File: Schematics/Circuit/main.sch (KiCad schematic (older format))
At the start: 49 parts

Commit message: Edit schematic and model
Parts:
- removed C?: 2.2 nF, ~, symbol C
- removed C?: 0.8 uF, ~, symbol C
- removed C?: 100 nF, ~, symbol C
- removed C?: 10 nF, ~, symbol C
- removed IC?: MPU-6050, ~, symbol MPU-6050
- removed R?: 4k7, ~, symbol R
- added J1, J2, J3, J4, J5: Conn_01x07, symbol Conn_01x07
- added R10, R11, R12, R13, R5, R6, R7, R8: 10k, symbol R
- added R14, R16, R18: 2k2, symbol R
- added R15, R17, R19: 2k8, symbol R
- C1, C10, C11, C12, C13, C2, C3, C4, C5, C8, C9: renamed from C?; symbol C -> C-RESCUE-main
- C6, C7: renamed from C?; value 22 pF -> 20 pF; symbol C -> C-RESCUE-main
- R1, R4: renamed from R?; symbol R -> R-RESCUE-main
- R2, R3: renamed from R?; value 4k7 -> 2k; symbol R -> R-RESCUE-main
- gave numbers to parts that had none: 26
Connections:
- net labels added: INT1, INT2, INT3, INT4, LED-TOP, LED1, LED2, LED3, LED4, PWRKEY, RXD-GSM, SLEEP-GSM, TXD-GSM, XSHUT1, XSHUT2, XSHUT3, XSHUT4
- wire segments 144 -> 170
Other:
- moved on the sheet: C10, C11, C12, C13, C6, C7, CSTECE1, IC3, P18, P19, R4

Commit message: Edit schematic and footprints
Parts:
- added J1: Conn_01x03, Pin_Headers:Pin_Header_Straight_1x03_Pitch2.54mm, symbol Conn_01x03
- C1, C3, C5, C8: footprint ~ -> Capacitors_Tantalum_SMD:CP_Tantalum_Case-C_EIA-6032-28_Hand
- C10, C11, C12, C13, C2, C4, C9: footprint ~ -> Capacitors_SMD:C_0805_HandSoldering
- C6, C7: footprint ~ -> Capacitors_SMD:C_0402
- CSTECE1: footprint ~ -> Crystals:Crystal_SMD_SeikoEpson_MA505-2pin_12.7x5.1mm_HandSoldering
- D1: footprint ~ -> Diodes_SMD:D_MiniMELF_Handsoldering
- IC1, IC2: footprint (none) -> CanSat:ncp1117
- IC3: footprint TQFP100 -> ATMEGA2560-16AU:QFP50P1600X1600X120-100N
- J2: renamed from J1; footprint (none) -> Pin_Headers:Pin_Header_Straight_1x07_Pitch2.54mm
- J3: renamed from J2; footprint (none) -> Pin_Headers:Pin_Header_Straight_1x07_Pitch2.54mm
- J4: renamed from J3; footprint (none) -> Pin_Headers:Pin_Header_Straight_1x07_Pitch2.54mm
- J5: renamed from J4; footprint (none) -> Pin_Headers:Pin_Header_Straight_1x07_Pitch2.54mm
- J6: renamed from J5; footprint (none) -> Pin_Headers:Pin_Header_Straight_1x07_Pitch2.54mm
- K1, K2: footprint (none) -> CanSat:SMD_6pin_IC
- P1, P10, P11, P12, P13, P14, P15, P16, P2, P3, P4, P5, P6, P7, P8, P9: footprint (none) -> Pin_Headers:Pin_Header_Straight_1x02_Pitch2.54mm
- P17: footprint (none) -> Pin_Headers:Pin_Header_Straight_2x05_Pitch2.00mm
- P18: footprint (none) -> CanSat:co2
- P19: footprint (none) -> Pin_Headers:Pin_Header_Straight_1x04_Pitch2.54mm
- R1, R2, R3, R4: footprint ~ -> Resistors_SMD:R_0603
- R10: renamed from R11; footprint (none) -> Resistors_SMD:R_0603
- R11: renamed from R12; footprint (none) -> Resistors_SMD:R_0603
- R12: renamed from R13; footprint (none) -> Resistors_SMD:R_0603
- R13: renamed from R14; footprint (none) -> Resistors_SMD:R_0805
- R14: renamed from R15; footprint (none) -> Resistors_SMD:R_0603
- R15: renamed from R16; footprint (none) -> Resistors_SMD:R_0805
- R16: renamed from R17; footprint (none) -> Resistors_SMD:R_0603
- R17: renamed from R18; footprint (none) -> Resistors_SMD:R_0805
- R18: renamed from R19; footprint (none) -> Resistors_SMD:R_0603
- R5, R6, R7, R8: footprint (none) -> Resistors_SMD:R_0603
- R9: renamed from R10; footprint (none) -> Resistors_SMD:R_0603
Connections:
- net labels added: SERVO
- wire segments 170 -> 178

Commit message: Edit finish circuits and some model work
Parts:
- removed P17: CONN_9, Pin_Headers:Pin_Header_Straight_2x05_Pitch2.00mm, symbol CONN_9
- added C14: 100 nF, Capacitors_SMD:C_0805, symbol C-RESCUE-main
- added IC4: RFM69HW, RFM69HW:XCVR_RFM95W-868S2, symbol RFM69HW
- added J10: Conn_01x04, CanSat:MOLEX_PicoBlade_4, symbol Conn_01x04
- added J7: Conn_01x05, Pin_Headers:Pin_Header_Straight_1x05_Pitch1.27mm_SMD_Pin1Right, symbol Conn_01x05
- added J8: Conn_02x05_Counter_Clockwise, Pin_Headers:Pin_Header_Straight_2x05_Pitch1.00mm_SMD, symbol Conn_02x05_Counter_Clockwise
- added J9: Conn_01x06, CanSat:MOLEX_PicoBlade_6, symbol Conn_01x06
- added P17, P20, P21: CONN_2, CanSat:MOLEX_PicoBlade_2, symbol CONN_2
- added Q1, Q2, Q3, Q4, Q5, Q6: BSS138, TO_SOT_Packages_SMD:SOT-23, symbol BSS138
- added R19, R20, R21, R22, R24, R25, R26, R28, R29, R30, R31, R32: 10k, Resistors_SMD:R_0603, symbol R
- added R23: 2k2, Resistors_SMD:R_0805, symbol R
- added R27: 2k8, Resistors_SMD:R_0603, symbol R
- added R33: 20k, Resistors_SMD:R_0603, symbol R-RESCUE-main
- added R34: 10k, Resistors_SMD:R_0603, symbol R-RESCUE-main
- C1: footprint Capacitors_Tantalum_SMD:CP_Tantalum_Case-C_EIA-6032-28_Hand -> Capacitors_Tantalum_SMD:CP_Tantalum_Case-U_EIA-6032-15_Reflow
- C10, C11, C12, C13, C2, C4, C9: footprint Capacitors_SMD:C_0805_HandSoldering -> Capacitors_SMD:C_0805
- C3, C5, C8: footprint Capacitors_Tantalum_SMD:CP_Tantalum_Case-C_EIA-6032-28_Hand -> Capacitors_Tantalum_SMD:CP_Tantalum_Case-C_EIA-6032-28_Reflow
- CSTECE1: footprint Crystals:Crystal_SMD_SeikoEpson_MA505-2pin_12.7x5.1mm_HandSoldering -> CanSat:Crystal_SMD
- D1: footprint Diodes_SMD:D_MiniMELF_Handsoldering -> Diodes_SMD:D_MiniMELF
- IC3: footprint ATMEGA2560-16AU:QFP50P1600X1600X120-100N -> CanSat:AtMega2560-AU
- J1: footprint Pin_Headers:Pin_Header_Straight_1x03_Pitch2.54mm -> MOLEX_PicoBlade_3:MOLEX_0532610371
- J2, J3, J4, J5, J6: footprint Pin_Headers:Pin_Header_Straight_1x07_Pitch2.54mm -> CanSat:MOLEX_PicoBlade_7
- P1, P10, P11, P12, P13, P14, P15, P16, P2, P3, P4, P5, P6, P7, P8, P9: footprint Pin_Headers:Pin_Header_Straight_1x02_Pitch2.54mm -> CanSat:MOLEX_PicoBlade_2
- P19: footprint Pin_Headers:Pin_Header_Straight_1x04_Pitch2.54mm -> CanSat:MOLEX_PicoBlade_4
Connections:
- net labels added: DTR, LED_TOP, MISO, MOSI, PWM1, PWM2, PWM3, PWM4, PWM5, PWM6, PWM7, PWM8, RFMINT, RFM_INT, SCK, SS, V_READ
- net labels removed: FC_IN, FC_OUT, LED, LED-TOP
- wire segments 178 -> 247
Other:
- moved on the sheet: J1, J2, K1, P18, P19, R13, R14, R15, R16, R17, R18

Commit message: Edit pcb and model
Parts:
- added J11: Conn_01x04, CanSat:MOLEX_PicoBlade_4, symbol Conn_01x04
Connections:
- net labels added: RX_GPS, TX_GPS
- wire segments 247 -> 253
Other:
- moved on the sheet: J1
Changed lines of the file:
@@
 	1    0    0    -1
 $EndComp
-Text Label 4200 5400 0    60   ~ 0
+Text Label 7100 5400 0    60   ~ 0
 TX
-Text Label 4200 5300 0    60   ~ 0
+Text Label 7100 5300 0    60   ~ 0
 RX
 Text Label 7050 4500 0    60   ~ 0
@@
 Text Label 10400 3000 0    60   ~ 0
 SLEEP-GSM
-Text Label 7050 5400 0    60   ~ 0
+Text Label 3950 5400 0    60   ~ 0
 RXD-GSM
-Text Label 7050 5300 0    60   ~ 0
+Text Label 3950 5300 0    60   ~ 0
 TXD-GSM
 Text Label 7050 4800 0    60   ~ 0
@@
 L Conn_01x03 J1
 U 1 1 5A54080E
-P 3900 4200
-F 0 "J1" H 3900 4400 50  0000 C CNN
-F 1 "Conn_01x03" H 3900 4000 50  0000 C CNN
-F 2 "MOLEX_PicoBlade_3:MOLEX_0532610371" H 3900 4200 50  0001 C CNN
-F 3 "" H 3900 4200 50  0001 C CNN
-	1    3900 4200
+P 3750 4200
+F 0 "J1" H 3750 4400 50  0000 C CNN
+F 1 "Conn_01x03" H 3750 4000 50  0000 C CNN
+F 2 "MOLEX_PicoBlade_3:MOLEX_0532610371" H 3750 4200 50  0001 C CNN
+F 3 "" H 3750 4200 50  0001 C CNN
+	1    3750 4200
 	1    0    0    -1
 $EndComp
@@
 L +5V #PWR049
 U 1 1 5A540AD7
-P 3450 4200
-F 0 "#PWR049" H 3450 4050 50  0001 C CNN
-F 1 "+5V" H 3450 4340 50  0000 C CNN
-F 2 "" H 3450 4200 50  0001 C CNN
-F 3 "" H 3450 4200 50  0001 C CNN
-	1    3450 4200
+P 3300 4200
+F 0 "#PWR049" H 3300 4050 50  0001 C CNN
+F 1 "+5V" H 3300 4340 50  0000 C CNN
+F 2 "" H 3300 4200 50  0001 C CNN
+F 3 "" H 3300 4200 50  0001 C CNN
+	1    3300 4200
 	0    -1   -1   0
 $EndComp
@@
 L GND #PWR050
 U 1 1 5A540B69
-P 3600 4300
-F 0 "#PWR050" H 3600 4050 50  0001 C CNN
-F 1 "GND" H 3600 4150 50  0000 C CNN
-F 2 "" H 3600 4300 50  0001 C CNN
-F 3 "" H 3600 4300 50  0001 C CNN
-	1    3600 4300
-	0    1    1    0
-$EndComp
-Text Label 3350 4100 0    60   ~ 0
+P 3450 4300
+F 0 "#PWR050" H 3450 4050 50  0001 C CNN
+F 1 "GND" H 3450 4150 50  0000 C CNN
+F 2 "" H 3450 4300 50  0001 C CNN
+F 3 "" H 3450 4300 50  0001 C CNN
+	1    3450 4300
+	0    1    1    0
+$EndComp
+Text Label 3200 4100 0    60   ~ 0
 SERVO
 Text Label 7050 3300 0    60   ~ 0
@@
 	1550 1850 1550 1900
 Wire Wire Line
-	4200 5300 4400 5300
-Wire Wire Line
-	4200 5400 4400 5400
+	7000 5300 7200 5300
+Wire Wire Line
+	7000 5400 7200 5400
 Wire Wire Line
 	7000 4400 7200 4400
@@
 	10400 3000 10900 3000
 Wire Wire Line
-	7000 5300 7500 5300
-Wire Wire Line
-	7000 5400 7500 5400
+	3900 5300 4400 5300
+Wire Wire Line
+	3900 5400 4400 5400
 Wire Wire Line
 	7000 2200 7400 2200
@@
 	7000 4100 7300 4100
 Wire Wire Line
-	3700 4100 3350 4100
-Wire Wire Line
-	3600 4300 3700 4300
-Wire Wire Line
-	3700 4200 3450 4200
+	3550 4100 3200 4100
+Wire Wire Line
+	3450 4300 3550 4300
+Wire Wire Line
+	3550 4200 3300 4200
 Wire Wire Line
 	7000 3300 7350 3300
@@
 Wire Wire Line
 	7400 3100 7000 3100
+$Comp
+L Conn_01x04 J11
+U 1 1 5A5EABAA
+P 9650 1800
+F 0 "J11" H 9650 2000 50  0000 C CNN
+F 1 "Conn_01x04" H 9650 1500 50  0000 C CNN
+F 2 "CanSat:MOLEX_PicoBlade_4" H 9650 1800 50  0001 C CNN
+F 3 "" H 9650 1800 50  0001 C CNN
+	1    9650 1800
+	1    0    0    -1
+$EndComp
+$Comp
+L +5V #PWR080
+U 1 1 5A5EAF9D
+P 9150 1700
+F 0 "#PWR080" H 9150 1550 50  0001 C CNN
+F 1 "+5V" H 9150 1840 50  0000 C CNN
+F 2 "" H 9150 1700 50  0001 C CNN
+F 3 "" H 9150 1700 50  0001 C CNN
+	1    9150 1700
+	0    -1   -1   0
+$EndComp
+$Comp
+L GND #PWR081
+U 1 1 5A5EB196
+P 9100 1800
+F 0 "#PWR081" H 9100 1550 50  0001 C CNN
+F 1 "GND" H 9100 1650 50  0000 C CNN
+F 2 "" H 9100 1800 50  0001 C CNN
+F 3 "" H 9100 1800 50  0001 C CNN
+	1    9100 1800
+	0    1    1    0
+$EndComp
+Wire Wire Line
+	9150 1700 9450 1700
+Wire Wire Line
+	9100 1800 9450 1800
+Text Label 9100 1900 0    60   ~ 0
+TX_GPS
+Text Label 9100 2000 0    60   ~ 0
+RX_GPS
+Wire Wire Line
+	9100 1900 9450 1900
+Wire Wire Line
+	9100 2000 9450 2000
+Text Label 4050 4400 0    60   ~ 0
+RX_GPS
+Text Label 4050 4500 0    60   ~ 0
+TX_GPS
+Wire Wire Line
+	4050 4400 4400 4400
+Wire Wire Line
+	4400 4500 4050 4500
 $EndSCHEMATC

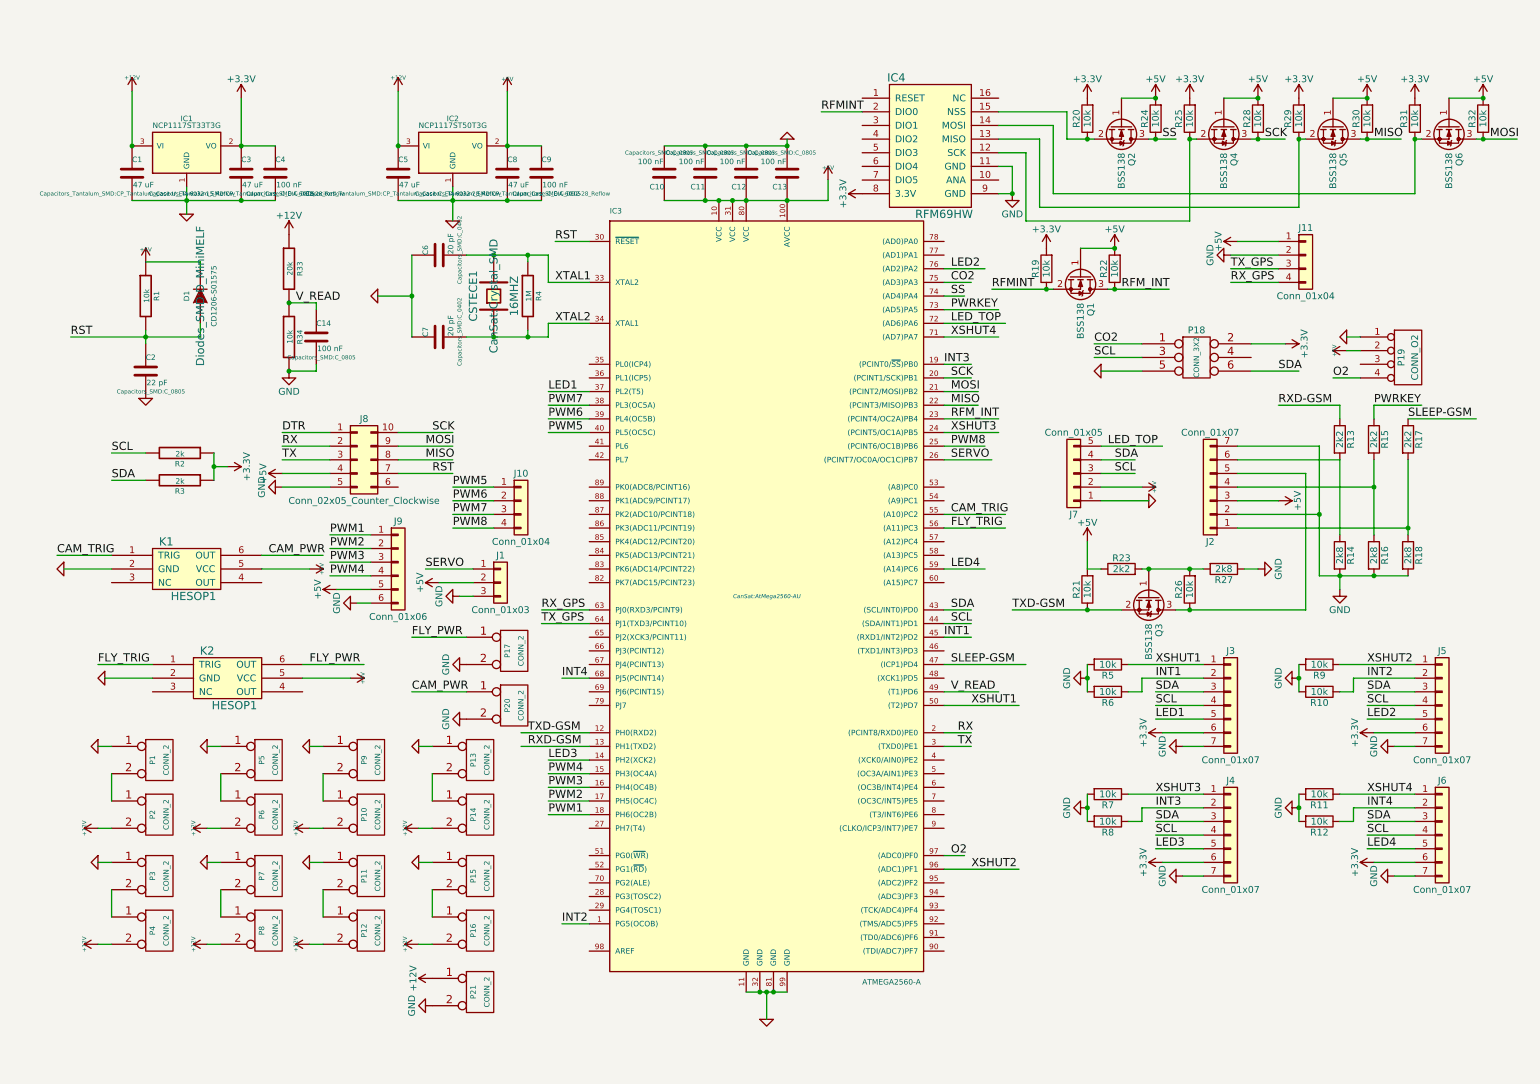
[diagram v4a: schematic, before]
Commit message: Edit schematic and model, add images
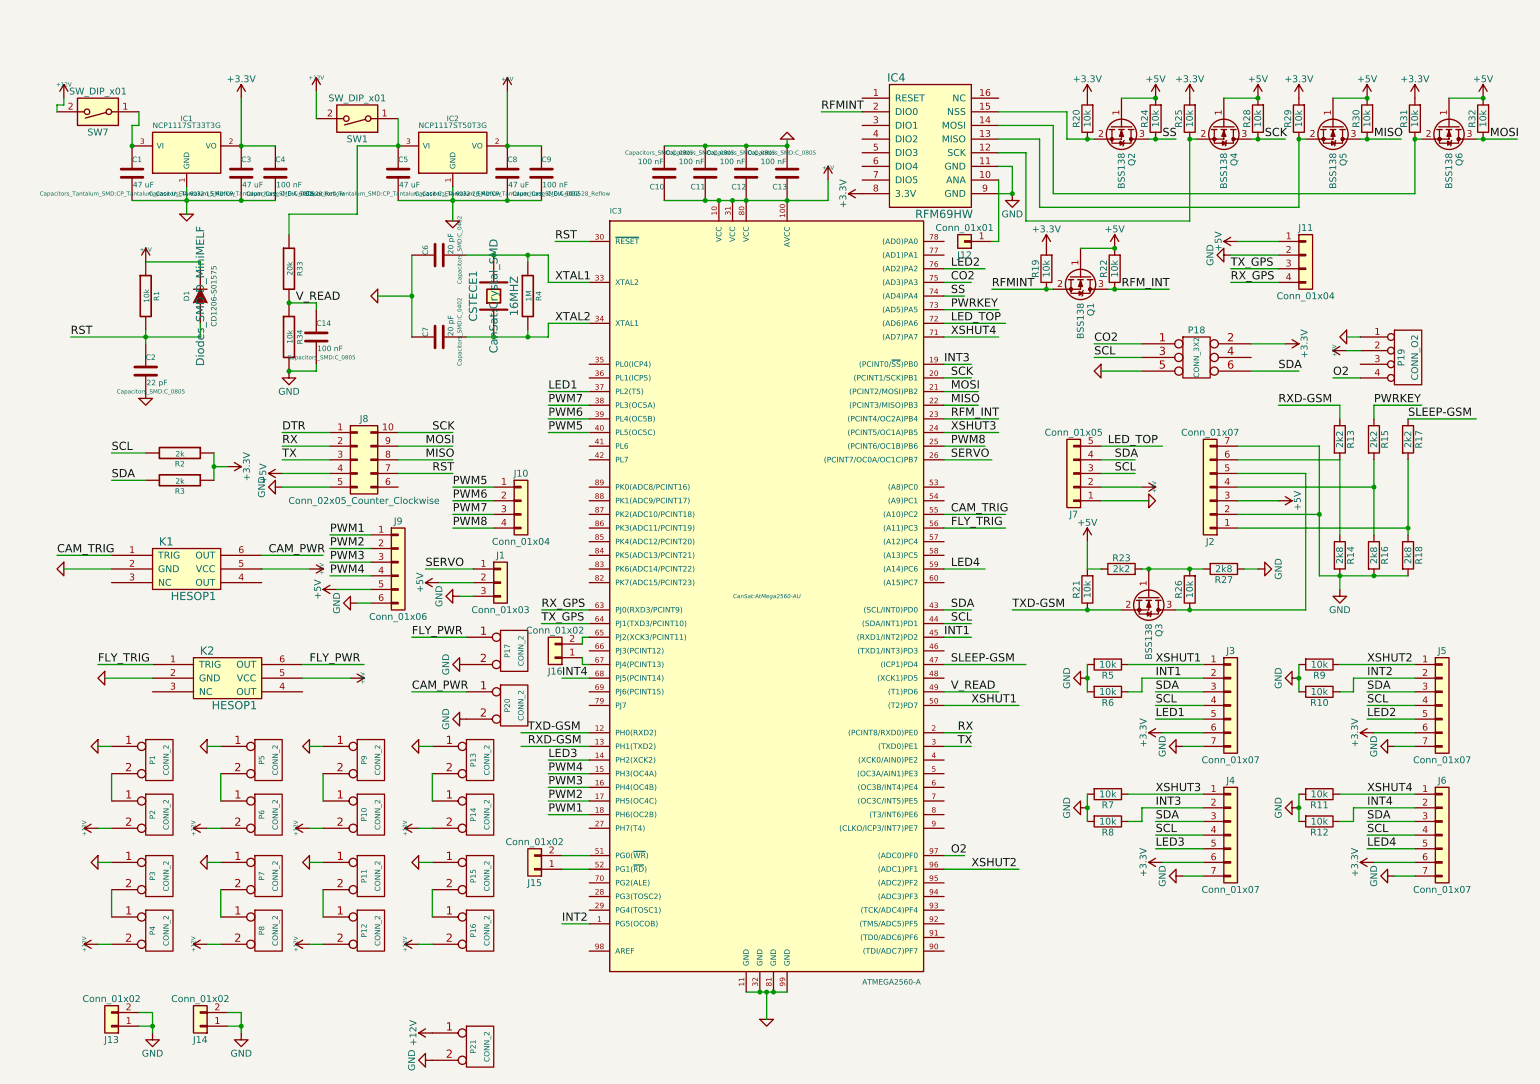
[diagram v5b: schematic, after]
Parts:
- added J12: Conn_01x01, Pin_Headers:Pin_Header_Straight_1x01_Pitch2.54mm, symbol Conn_01x01
- added J13, J14, J15, J16: Conn_01x02, CanSat:MOLEX_PicoBlade_2, symbol Conn_01x02
- added SW1, SW7: SW_DIP_x01, CanSat:Switch, symbol SW_DIP_x01
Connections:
- wire segments 253 -> 277
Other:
- moved on the sheet: P21
